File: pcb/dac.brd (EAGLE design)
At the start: 66 x 63.5 mm, 23 parts, among them U1 PIC16F1773-I/SP, U2 MCP6002-I/P

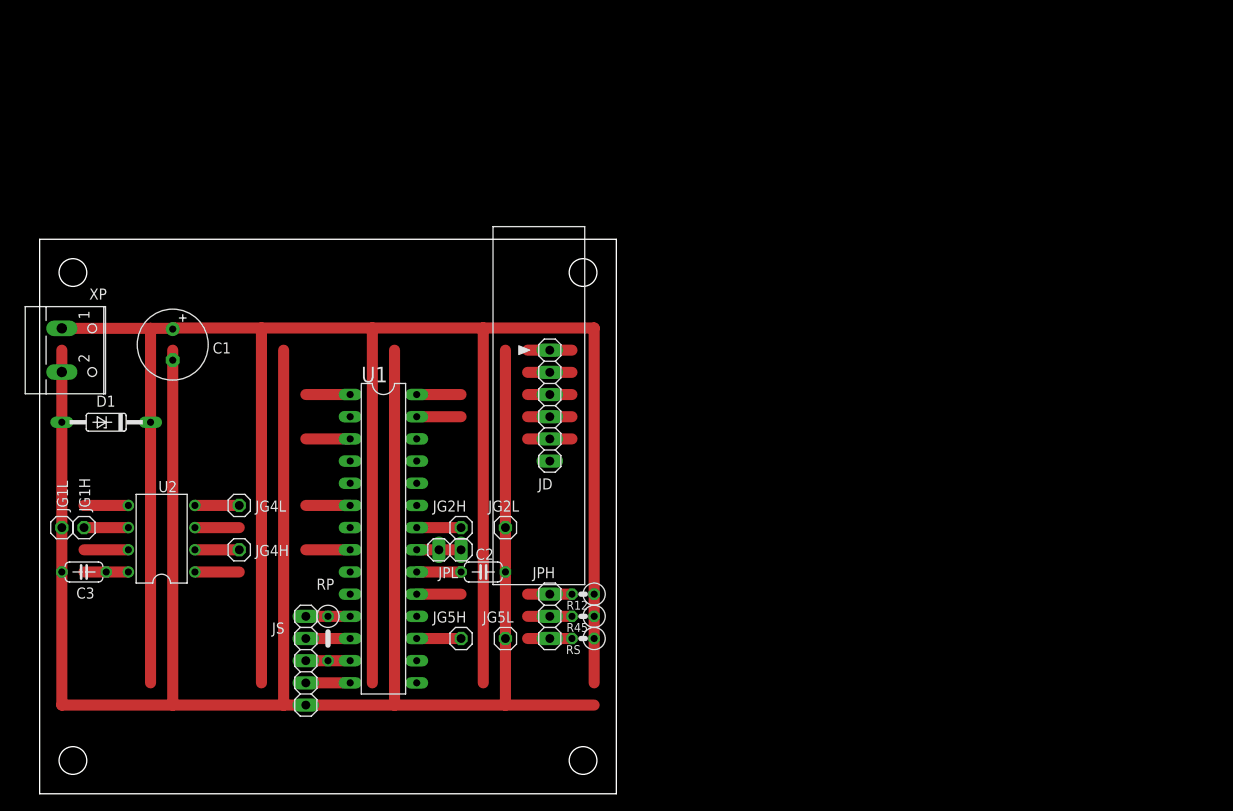
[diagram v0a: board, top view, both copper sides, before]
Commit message: New layout with larger board and level shifter
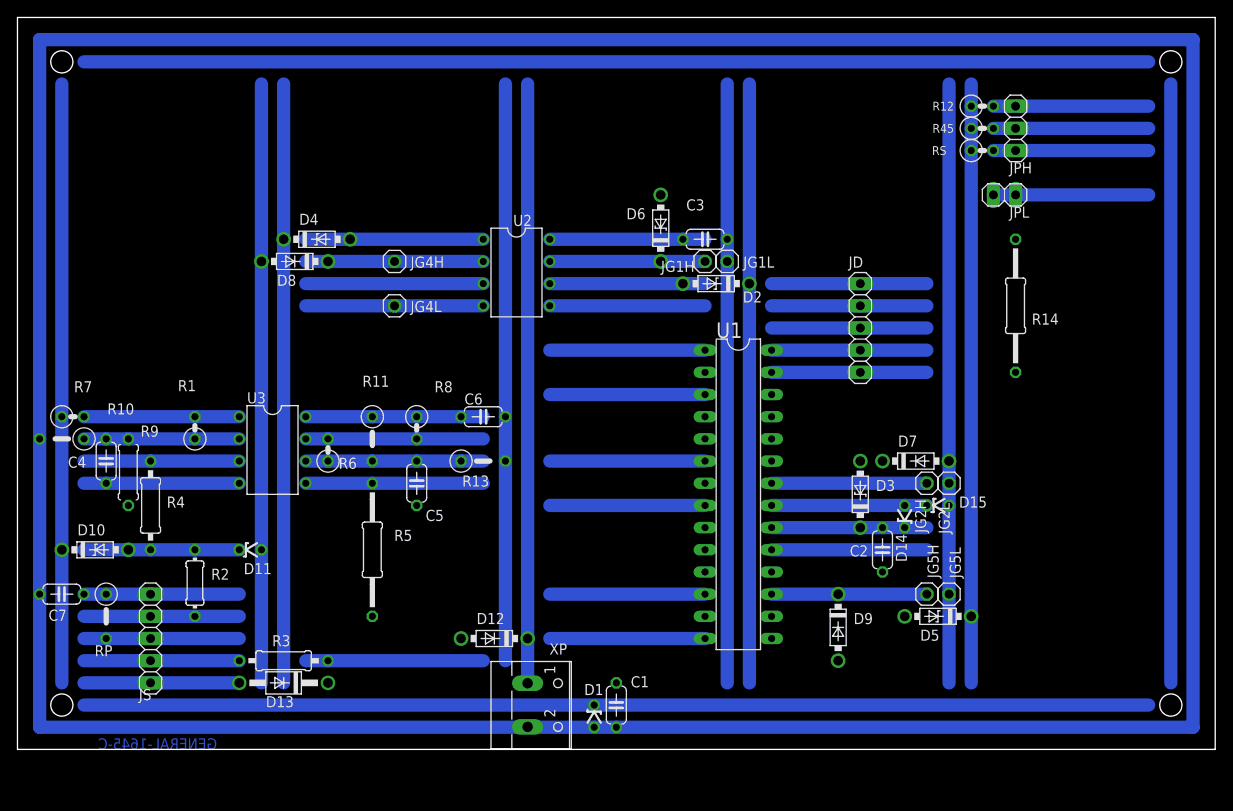
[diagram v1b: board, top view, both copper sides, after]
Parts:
- added C4, C5: 100p, rcl:C050-024X044
- added C6: 2.2uF, rcl:C050-024X044
- added C7: 2.2u, rcl:C050-024X044
- added D10: 1N5817-H76, diode-vertical:DO41-7.6
- added D11: 1N5817-V, diode-vertical:ZDIO-2.5
- added D12: 1N5817-T, diode:DO41-7.6
- added D13: 1N5817, diode-vertical:DO41-10
- added D14, D15: SB140TA, diode-vertical:ZDIO-2.5
- added D2, D3, D4, D5, D6: SB140TA, diode-vertical:DO41-7.6
- added D7, D8, D9: SB140TA, diode:DO41-7.6
- added R1, R6: 330k, rcl:0207/2V
- added R10, R11, R13: 10k, rcl:0207/5V
- added R14: 8R, rcl:0207/15
- added R2: 1k, rcl:0204/7
- added R3: 1k, rcl:0207/10
- added R4: 56k, rcl:0207/10
- added R5: 56k, rcl:0207/15
- added R7, R8: 10k, rcl:0207/2V
- added R9: 10k, rcl:0207/7
- added U3: KA393, linear:DIL08
- C1: value 470uF -> 2.2uF; device rcl:E3,5-8 -> rcl:C050-024X044
- D1: device diode:DO35Z10 -> diode-vertical:ZDIO-2.5
- JD: device pinhd-pol:1X06-PICKIT -> pinhead:1X05
- R12, R45: value 38R -> 24R
- moved JG1L 82.1 mm to (78.7, 53.3), turned to 180 degrees
- moved C3 80.7 mm to (76.2, 55.9), turned to 0 degrees
- moved JG1H 77.4 mm to (76.2, 53.3)
- moved JPH 77.3 mm to (111.8, 68.6)
- moved JPL 75.4 mm to (110.5, 61.0)
- moved R12 72.2 mm to (108.0, 71.1), turned to 0 degrees
- moved R45 72.2 mm to (108.0, 68.6), turned to 0 degrees
- moved RS 72.2 mm to (108.0, 66.0), turned to 0 degrees
- moved XP 67.1 mm to (57.1, 2.54)
- moved C1 65.5 mm to (66.0, 2.54)
- moved D1 65.2 mm to (63.5, 1.27), turned to 270 degrees
- moved JG2H 53.6 mm to (101.6, 27.9)
- moved JG5H 53.6 mm to (101.6, 15.2)
- moved JG2L 51.1 mm to (104.1, 27.9)
- moved JG5L 51.1 mm to (104.1, 15.2)
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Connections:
- removed net FADE: JPL.1, JPL.2, U1.21
- new net !FADE: D14.A, D15.C, R14.1, U1.21
- new net !FADE_PROT: JPL.1, JPL.2, R14.2
- new net MISO_LINE: JS.3, RP.2
- new net MOSI_LINE: JS.2, R2.1
- new net MOSI_N: C4.1, R1.1, R10.1, R9.2, U3.2
- new net MOSI_P: R4.2, U3.3
- new net MOSI_PROT: D10.A, D11.C, R2.2, R4.1
- new net SCLK_LINE: JS.4, R3.1
- new net SCLK_N: C5.1, R11.2, R13.1, R6.1, U3.6
- new net SCLK_P: R5.2, U3.5
- new net SCLK_PROT: D12.A, D13.C, R3.2, R5.1
- net +3V3: now also C7.1; no longer U1.11
- net +5V: now also C1.1, C6.1, D10.C, D12.C, D14.C, D2.C, D3.C, D4.C, D5.C, R11.1, R7.1, R8.1, R9.1, U3.8; no longer C1.+
- net DAC1: now also D2.A, D6.C
- net DAC2: now also D3.A, D7.C
- net DAC4: now also D4.A, D8.C
- net DAC5: now also D5.A, D9.C
- net GND: now also C1.2, C4.2, C5.2, C6.2, C7.2, D11.A, D13.A, D15.A, D6.A, D7.A, D8.A, D9.A, R10.2, R13.2, U3.4; no longer C1.-
- net MISO: no longer JS.3, RP.2
- net MOSI: now also R1.2, R7.2, U3.1; no longer JS.2
- net SCLK: now also R6.2, R8.2, U3.7; no longer JS.4
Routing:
- net GND: track 284.5 -> 802.7 mm
- net +5V: track 279.6 -> 729.0 mm
- net SCLK: track 5.08 -> 38.1 mm
- net MOSI: track 5.08 -> 35.6 mm
- net DAC4: track 10.2 -> 40.6 mm
- net DAC4_UNBUF: track 10.2 -> 38.1 mm
- net DAC1: track 10.2 -> 35.6 mm
- net !MCLR: track 10.2 -> 35.6 mm
- net DAC1_UNBUF: track 10.2 -> 35.6 mm
- net SCLK_PROT: track 0.00 -> 20.3 mm
- net SCLK_P: track 0.00 -> 20.3 mm
- net SCLK_N: track 0.00 -> 20.3 mm
- net SCLK_LINE: track 0.00 -> 17.8 mm
- net MOSI_PROT: track 0.00 -> 17.8 mm
- net MOSI_P: track 0.00 -> 17.8 mm
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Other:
- board size 66 x 63.5 mm -> 137.2 x 83.8 mm
- board text added: "Columns"
- board text added: "GENERAL-1645-C"
- board text added: "Rows"
- board text removed: "www.PROTO-ADVANTAGE.com SBB1605-1"

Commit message: MISO protection network, lower capacitance values, split jumper for LEDs
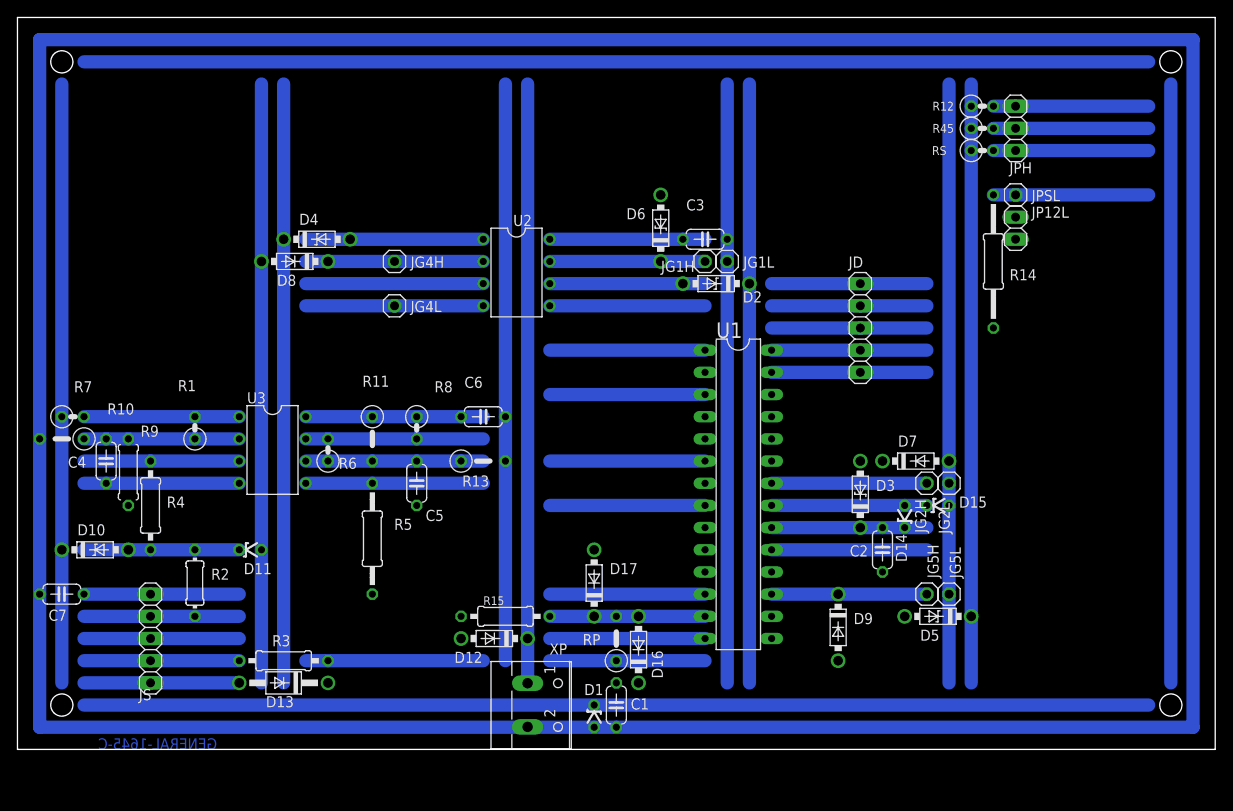
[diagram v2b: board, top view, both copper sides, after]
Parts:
- removed JPL: (no value), pinhead:1X02
- added D16, D17: 1N5817-T, diode:DO41-7.6
- added JP12L: (no value), pinhead:1X02
- added JPSL: (no value), pinhead:1X01
- added R15: 100R, rcl:0207/10
- C2, C3, C6: value 2.2uF -> 330nF
- C4, C5: value 100p -> 100pF
- C7: value 2.2u -> 330nF
- R10, R13: value 10k -> 22k
- R11, R9: value 10k -> 47k
- R5: device rcl:0207/15 -> rcl:0207/12
- moved RP 58.5 mm to (66.0, 10.2), turned to 90 degrees
- moved R14 5.68 mm to (109.2, 53.3)
- moved R5 1.27 mm to (38.1, 21.6)
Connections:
- net !FADE_PROT: now also JP12L.1, JP12L.2, JPSL.1; no longer JPL.1, JPL.2
- net +3V3: now also D16.C
- net GND: now also D17.A
- net MISO: now also D16.A, D17.C, R15.2, RP.2
- net MISO_LINE: now also R15.1; no longer RP.2
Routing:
- net MISO: track 0.00 -> 17.8 mm
- net +3V3: track 17.8 -> 35.6 mm
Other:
- board text added: "Move as needed (Eagle width limitation)"

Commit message: Replace screw terminals with more header
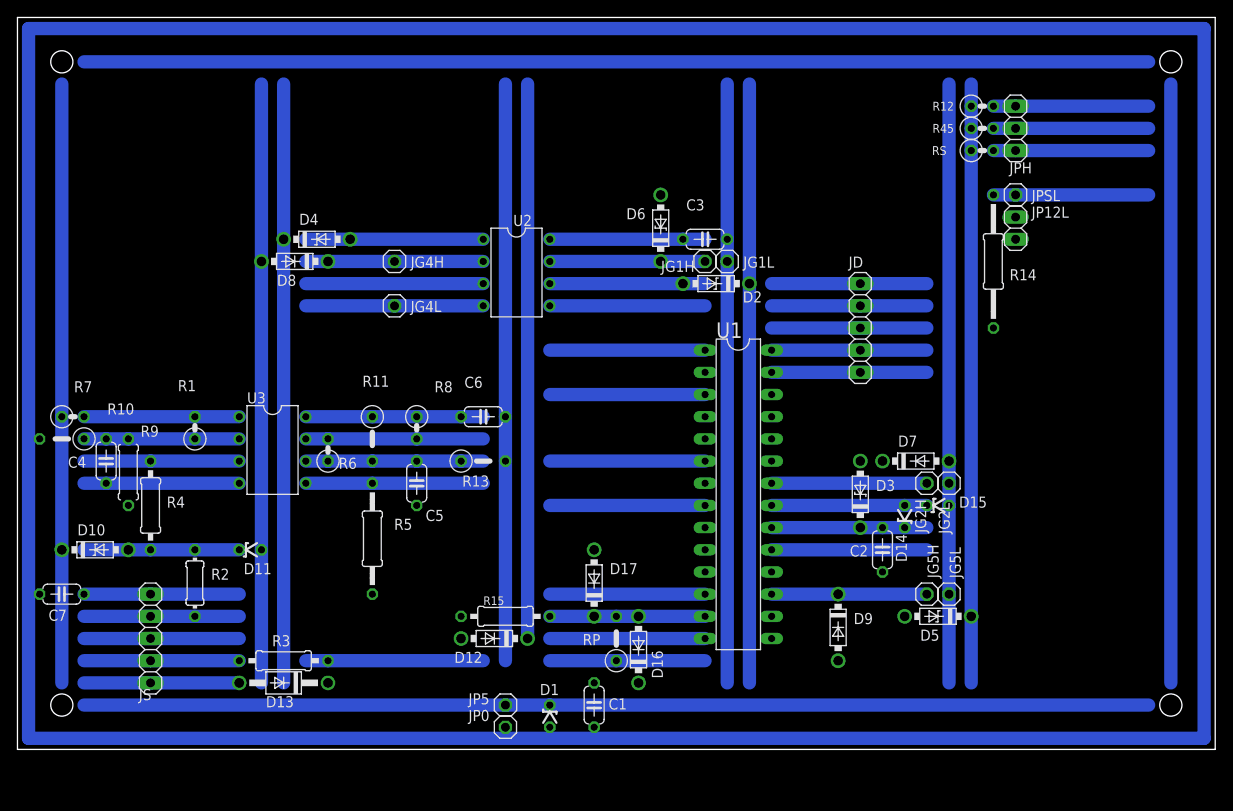
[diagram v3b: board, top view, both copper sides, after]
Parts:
- removed XP: (no value), con-wago-500:W237-102
- added JP0, JP5: (no value), pinhead:1X01
- moved D1 5.08 mm to (58.4, 1.27)
- moved C1 2.54 mm to (63.5, 2.54)
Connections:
- net +5V: now also JP5.1; no longer XP.1
- net GND: now also JP0.1; no longer XP.2
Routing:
- net GND: track 802.7 -> 812.8 mm
- net +5V: track 729.0 -> 723.9 mm
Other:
- board text added: "Move as needed (Eagle height limitation)"

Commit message: Used different protection diodes for LEDs
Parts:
- D14, D15: value SB140TA -> 1N5817
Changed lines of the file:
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@@
 <attribute name="VALUE" x="1.016" y="10.668" size="1.27" layer="27" ratio="10"/>
 </element>
-<element name="D14" library="diode-vertical" package="ZDIO-2.5" value="SB140TA" x="99.06" y="24.13" smashed="yes" rot="R90">
+<element name="D14" library="diode-vertical" package="ZDIO-2.5" value="1N5817" x="99.06" y="24.13" smashed="yes" rot="R90">
 <attribute name="NAME" x="99.314" y="18.923" size="1.27" layer="25" ratio="10" rot="R90"/>
 </element>
-<element name="D15" library="diode-vertical" package="ZDIO-2.5" value="SB140TA" x="102.87" y="25.4" smashed="yes">
+<element name="D15" library="diode-vertical" package="ZDIO-2.5" value="1N5817" x="102.87" y="25.4" smashed="yes">
 <attribute name="NAME" x="105.283" y="25.146" size="1.27" layer="25" ratio="10"/>
 </element>
